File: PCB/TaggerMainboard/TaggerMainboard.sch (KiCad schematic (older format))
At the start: 80 parts

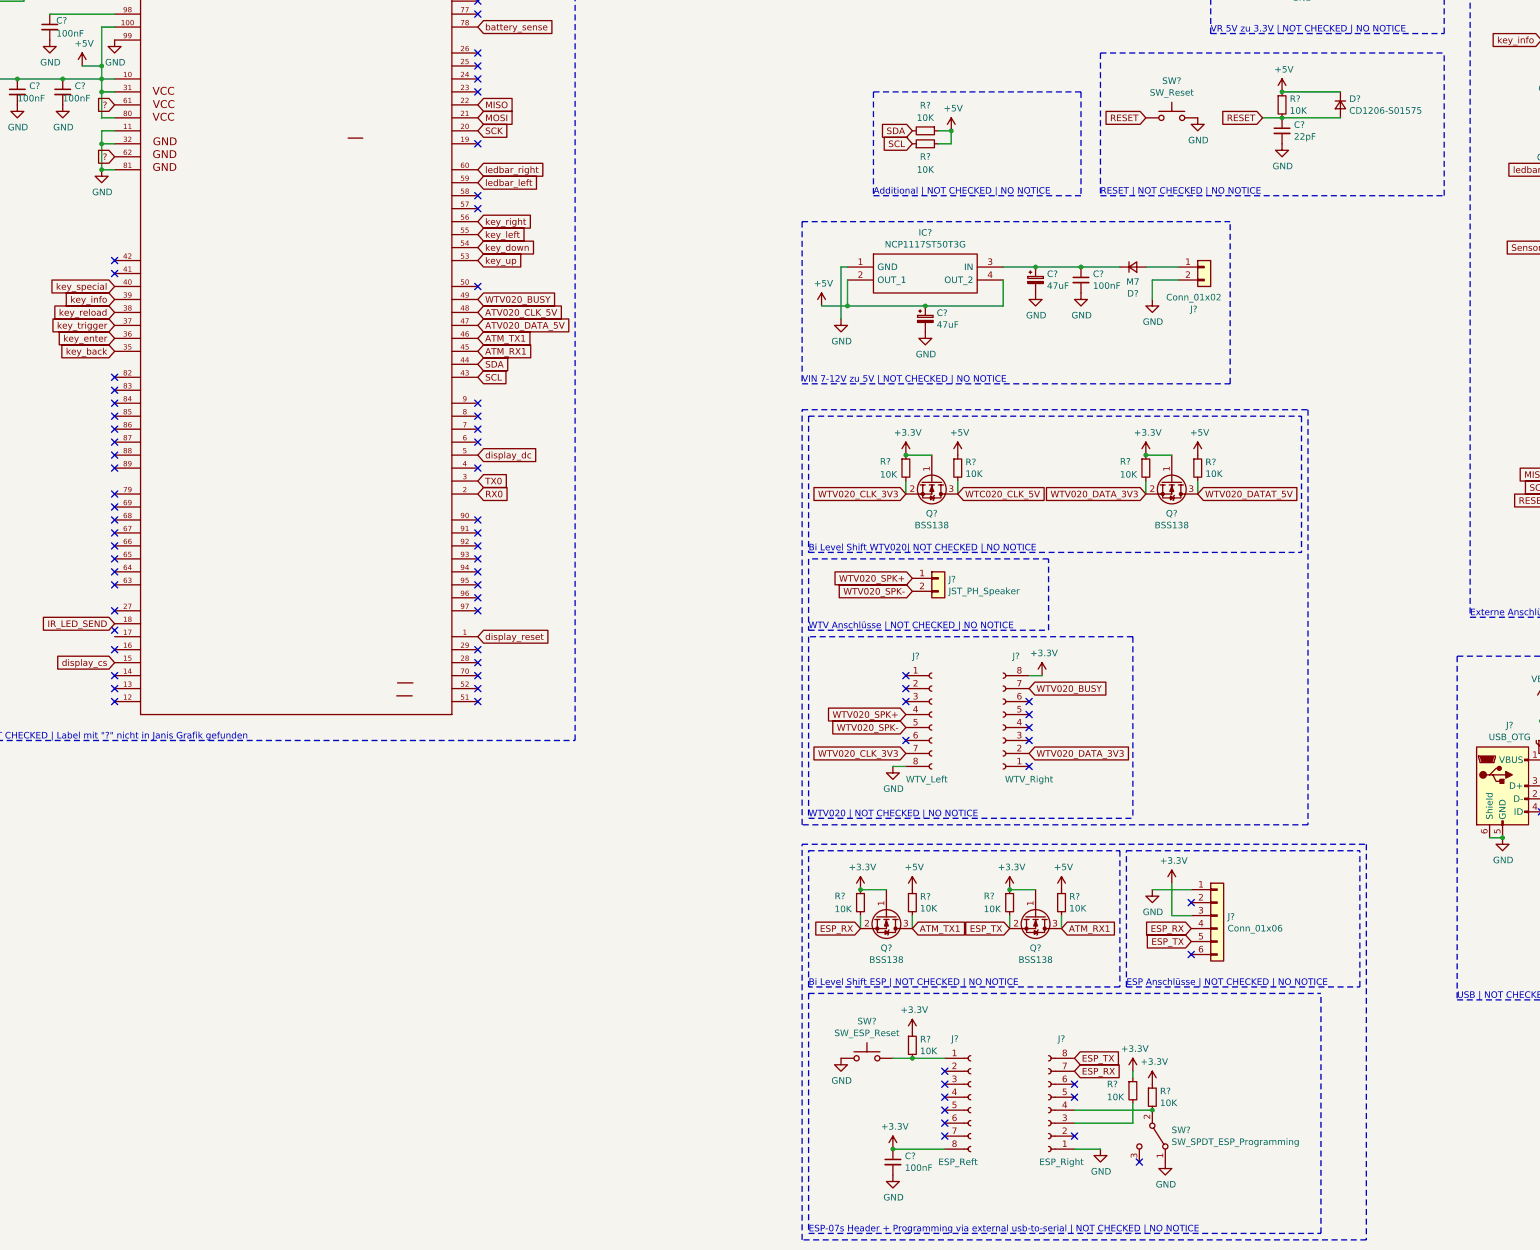
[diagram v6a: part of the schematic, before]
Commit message: VIN ersetzt + WiFi Entfernt + WiFi Header hinzugefügt
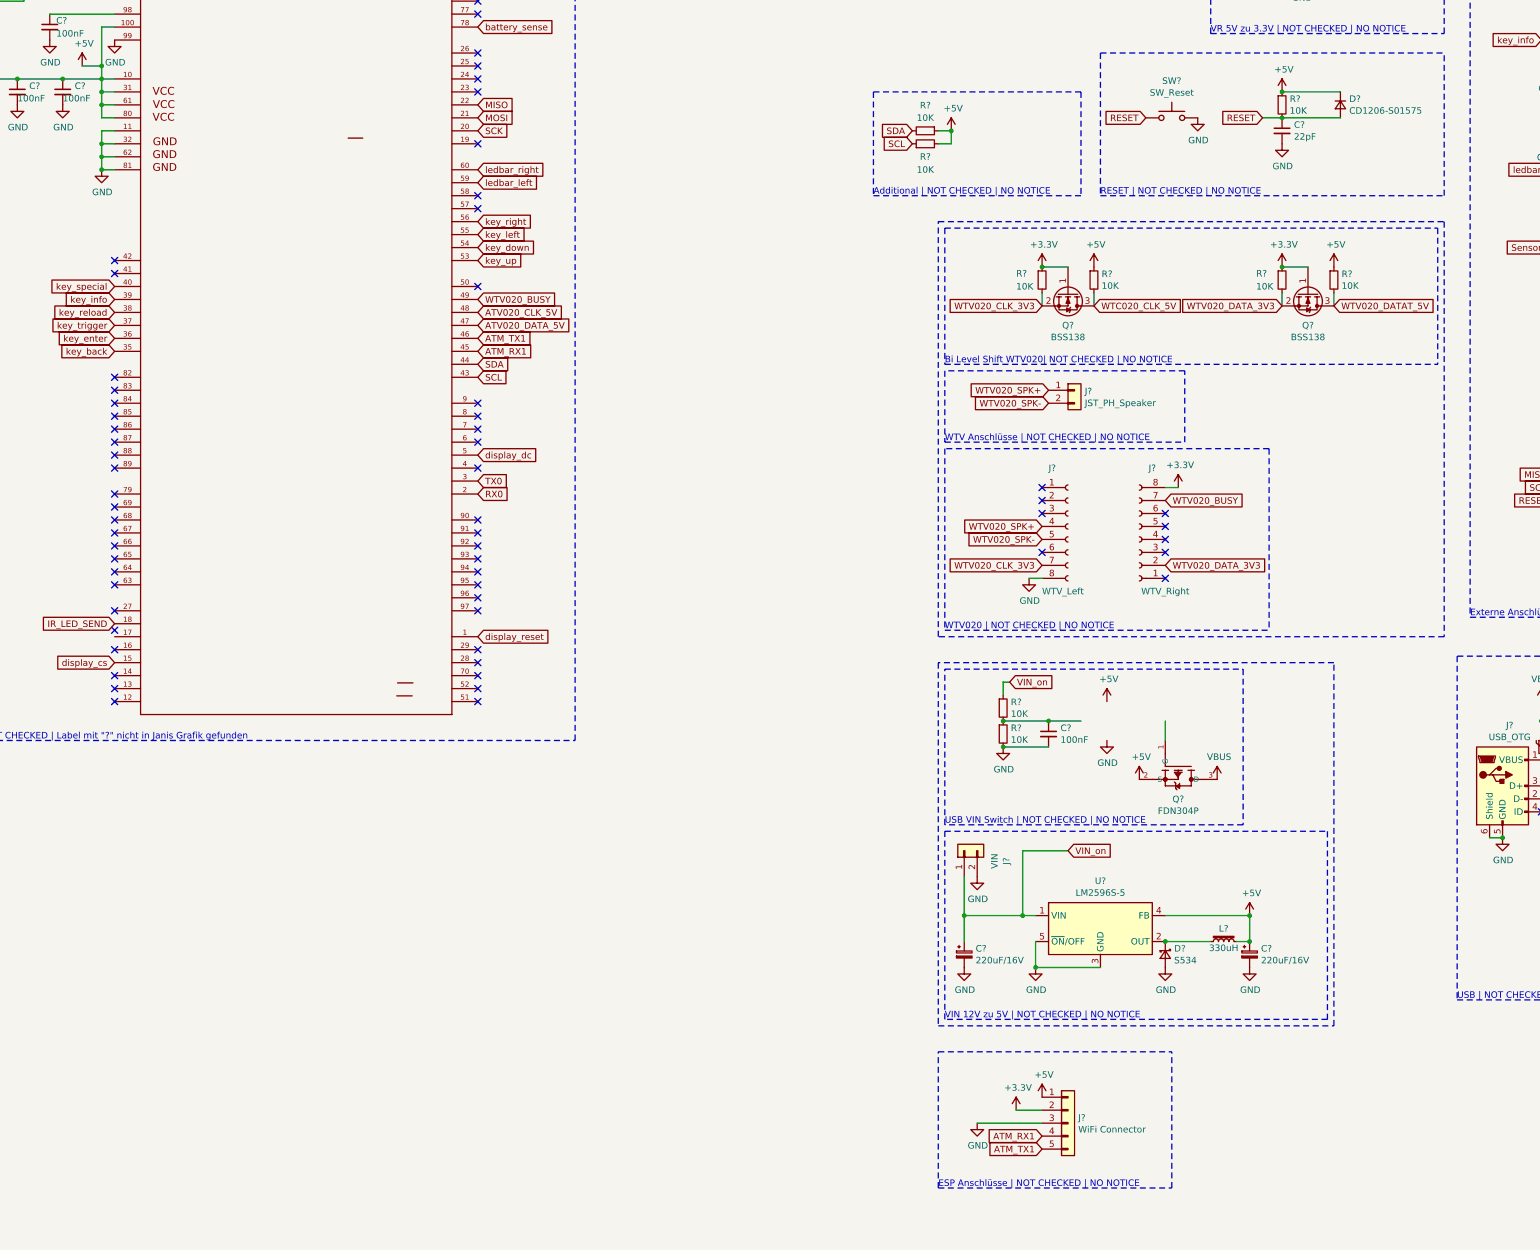
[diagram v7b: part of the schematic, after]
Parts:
- removed C? (x2): 100nF, Capacitor_SMD:C_0805_2012Metric, symbol Device:C_Small
- removed C? (x2): 47uF, Capacitor_SMD:CP_Elec_6.3x5.7, symbol Device:CP_Small
- removed D?: M7, Diode_SMD:D_0805_2012Metric, symbol Device:D_Small
- removed IC?: NCP1117ST50T3G, SOT230P700X180-4N, symbol Infinitag:NCP1117ST50T3G
- removed J?: ESP_Reft, symbol Connector:Conn_01x08_Female
- removed J?: ESP_Right, symbol Connector:Conn_01x08_Female
- removed J?: Conn_01x06, Connector_JST:JST_PH_B6B-PH-K_1x06_P2.00mm_Vertical, symbol Connector_Generic:Conn_01x06
- removed J?: Conn_01x02, Connector_JST:JST_PH_B2B-PH-K_1x02_P2.00mm_Vertical, symbol Connector_Generic:Conn_01x02
- removed Q? (x2): BSS138, Package_TO_SOT_SMD:SOT-23, symbol Transistor_FET:BSS138
- removed R? (x7): 10K, Resistor_SMD:R_0805_2012Metric, symbol Device:R_Small
- removed SW?: SW_ESP_Reset, Button_Switch_SMD:SW_SPST_FSMSM, symbol Switch:SW_Push
- removed SW?: SW_SPDT_ESP_Programming, symbol Switch:SW_SPDT
- added C? (x2): 220uF/16V, symbol Device:CP_Small
- added C?: 100nF, symbol Device:C_Small
- added D?: S534, symbol Device:D_Schottky_Small
- added J?: WiFi Connector, symbol Connector_Generic:Conn_01x05
- added J?: VIN, Connector_JST:JST_PH_B2B-PH-K_1x02_P2.00mm_Vertical, symbol Connector_Generic:Conn_01x02
- added L?: 330uH, symbol Device:L_Core_Iron_Small
- added Q?: FDN304P, SOT95P240X120-3N, symbol FDN340P:FDN340P
- added R? (x2): 10K, symbol Device:R_Small
- added U?: LM2596S-5, Package_TO_SOT_SMD:TO-263-5_TabPin3, symbol Regulator_Switching:LM2596S-5
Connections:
- net labels added: VIN_on
- net labels removed: ?, ESP_RX, ESP_TX
- wire segments 118 -> 112
- no-connect marks 90 -> 78
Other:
- note added: "USB VIN Switch | NOT CHECKED | NO NOTICE"
- note added: "VIN 12V zu 5V | NOT CHECKED | NO NOTICE"
- note removed: "Bi Level Shift ESP | NOT CHECKED | NO NOTICE"
- note removed: "ESP-07s Header + Programming via external usb-to-serial | NOT CHECKED | NO NOTICE"
- note removed: "VIN 7-12V zu 5V | NOT CHECKED | NO NOTICE"
- moved on the sheet: J?, Q?, R?

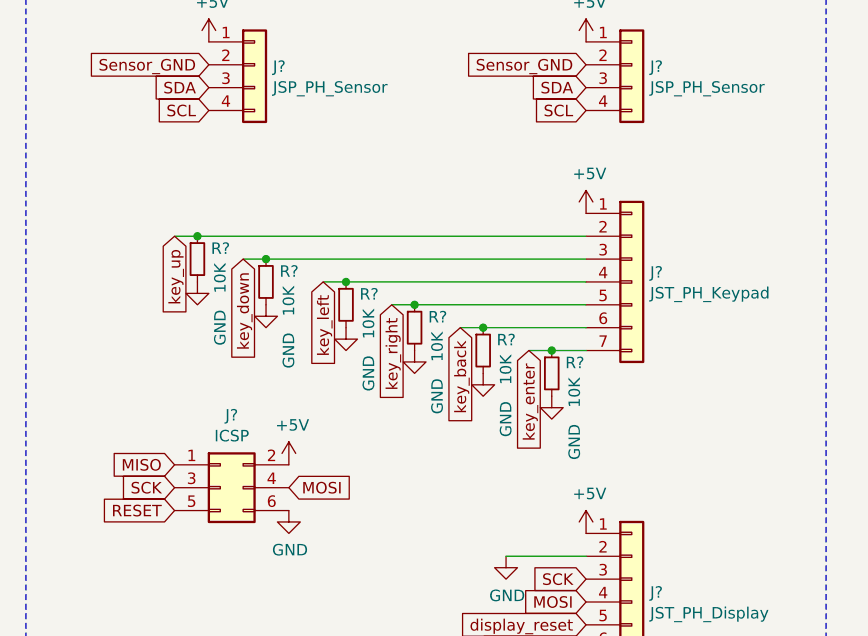
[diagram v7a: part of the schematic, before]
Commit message: Keypad ohne Widerstände auf dem Board
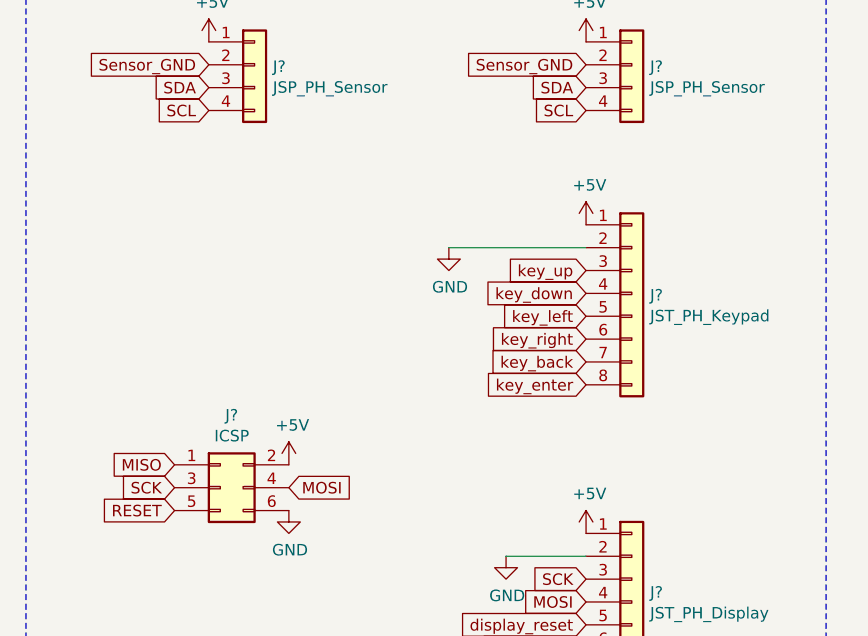
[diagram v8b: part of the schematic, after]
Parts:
- removed J?: JST_PH_Keypad, Connector_JST:JST_PH_B7B-PH-K_1x07_P2.00mm_Vertical, symbol Connector_Generic:Conn_01x07
- removed R? (x6): 10K, Resistor_SMD:R_0805_2012Metric, symbol Device:R_Small
- added J?: JST_PH_Keypad, symbol Connector_Generic:Conn_01x08
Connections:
- wire segments 112 -> 101
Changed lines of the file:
@@
 Text GLabel 13250 3650 0    50   Input ~ 0
 SCL
-$Comp
-L Connector_Generic:Conn_01x07 J?
-U 1 1 5C86ACB0
-P 15100 4400
-F 0 "J?" H 15180 4442 50  0000 L CNN
-F 1 "JST_PH_Keypad" H 15180 4351 50  0000 L CNN
-F 2 "Connector_JST:JST_PH_B7B-PH-K_1x07_P2.00mm_Vertical" H 15100 4400 50  0001 C CNN
-F 3 "~" H 15100 4400 50  0001 C CNN
-	1    15100 4400
-	1    0    0    -1
-$EndComp
-$Comp
-L Device:R_Small R?
-U 1 1 5C86ADDB
-P 14750 4800
-F 0 "R?" H 14809 4846 50  0000 L CNN
-F 1 "10K" V 14850 4650 50  0000 L CNN
-F 2 "Resistor_SMD:R_0805_2012Metric" H 14750 4800 50  0001 C CNN
-F 3 "~" H 14750 4800 50  0001 C CNN
-	1    14750 4800
-	1    0    0    -1
-$EndComp
-$Comp
-L power:GND #PWR?
-U 1 1 5C86AF22
-P 14750 4900
-F 0 "#PWR?" H 14750 4650 50  0001 C CNN
-F 1 "GND" V 14850 4700 50  0000 C CNN
-F 2 "" H 14750 4900 50  0001 C CNN
-F 3 "" H 14750 4900 50  0001 C CNN
-	1    14750 4900
-	1    0    0    -1
-$EndComp
-Text GLabel 14650 4700 3    50   Input ~ 0
+Text GLabel 14900 4850 0    50   Input ~ 0
 key_enter
-Wire Wire Line
-	14900 4700 14750 4700
-Wire Wire Line
-	14650 4700 14750 4700
-Connection ~ 14750 4700
-$Comp
-L Device:R_Small R?
-U 1 1 5C86EFD0
-P 14450 4700
-F 0 "R?" H 14509 4746 50  0000 L CNN
-F 1 "10K" V 14550 4550 50  0000 L CNN
-F 2 "Resistor_SMD:R_0805_2012Metric" H 14450 4700 50  0001 C CNN
-F 3 "~" H 14450 4700 50  0001 C CNN
-	1    14450 4700
-	1    0    0    -1
-$EndComp
-$Comp
-L power:GND #PWR?
-U 1 1 5C86EFD7
-P 14450 4800
-F 0 "#PWR?" H 14450 4550 50  0001 C CNN
-F 1 "GND" V 14550 4600 50  0000 C CNN
-F 2 "" H 14450 4800 50  0001 C CNN
-F 3 "" H 14450 4800 50  0001 C CNN
-	1    14450 4800
-	1    0    0    -1
-$EndComp
-Text GLabel 14350 4600 3    50   Input ~ 0
+Text GLabel 14900 4750 0    50   Input ~ 0
 key_back
-Wire Wire Line
-	14350 4600 14450 4600
-Connection ~ 14450 4600
-$Comp
-L Device:R_Small R?
-U 1 1 5C86F8EF
-P 14150 4600
-F 0 "R?" H 14209 4646 50  0000 L CNN
-F 1 "10K" V 14250 4450 50  0000 L CNN
-F 2 "Resistor_SMD:R_0805_2012Metric" H 14150 4600 50  0001 C CNN
-F 3 "~" H 14150 4600 50  0001 C CNN
-	1    14150 4600
-	1    0    0    -1
-$EndComp
-$Comp
-L power:GND #PWR?
-U 1 1 5C86F8F6
-P 14150 4700
-F 0 "#PWR?" H 14150 4450 50  0001 C CNN
-F 1 "GND" V 14250 4500 50  0000 C CNN
-F 2 "" H 14150 4700 50  0001 C CNN
-F 3 "" H 14150 4700 50  0001 C CNN
-	1    14150 4700
-	1    0    0    -1
-$EndComp
-Text GLabel 14050 4500 3    50   Input ~ 0
+Text GLabel 14900 4650 0    50   Input ~ 0
 key_right
-Wire Wire Line
-	14050 4500 14150 4500
-Connection ~ 14150 4500
-$Comp
-L Device:R_Small R?
-U 1 1 5C87034B
-P 13850 4500
-F 0 "R?" H 13909 4546 50  0000 L CNN
-F 1 "10K" V 13950 4350 50  0000 L CNN
-F 2 "Resistor_SMD:R_0805_2012Metric" H 13850 4500 50  0001 C CNN
-F 3 "~" H 13850 4500 50  0001 C CNN
-	1    13850 4500
-	1    0    0    -1
-$EndComp
-$Comp
-L power:GND #PWR?
-U 1 1 5C870352
-P 13850 4600
-F 0 "#PWR?" H 13850 4350 50  0001 C CNN
-F 1 "GND" V 13950 4400 50  0000 C CNN
-F 2 "" H 13850 4600 50  0001 C CNN
-F 3 "" H 13850 4600 50  0001 C CNN
-	1    13850 4600
-	1    0    0    -1
-$EndComp
-Text GLabel 13750 4400 3    50   Input ~ 0
+Text GLabel 14900 4550 0    50   Input ~ 0
 key_left
-Wire Wire Line
-	13750 4400 13850 4400
-Connection ~ 13850 4400
-$Comp
-L Device:R_Small R?
-U 1 1 5C870F04
-P 13500 4400
-F 0 "R?" H 13559 4446 50  0000 L CNN
-F 1 "10K" V 13600 4250 50  0000 L CNN
-F 2 "Resistor_SMD:R_0805_2012Metric" H 13500 4400 50  0001 C CNN
-F 3 "~" H 13500 4400 50  0001 C CNN
-	1    13500 4400
-	1    0    0    -1
-$EndComp
-$Comp
-L power:GND #PWR?
-U 1 1 5C870F0B
-P 13500 4500
-F 0 "#PWR?" H 13500 4250 50  0001 C CNN
-F 1 "GND" V 13600 4300 50  0000 C CNN
-F 2 "" H 13500 4500 50  0001 C CNN
-F 3 "" H 13500 4500 50  0001 C CNN
-	1    13500 4500
-	1    0    0    -1
-$EndComp
-Text GLabel 13400 4300 3    50   Input ~ 0
+Text GLabel 14900 4450 0    50   Input ~ 0
 key_down
-Wire Wire Line
-	13400 4300 13500 4300
-Connection ~ 13500 4300
-$Comp
-L Device:R_Small R?
-U 1 1 5C872016
-P 13200 4300
-F 0 "R?" H 13259 4346 50  0000 L CNN
-F 1 "10K" V 13300 4150 50  0000 L CNN
-F 2 "Resistor_SMD:R_0805_2012Metric" H 13200 4300 50  0001 C CNN
-F 3 "~" H 13200 4300 50  0001 C CNN
-	1    13200 4300
-	1    0    0    -1
-$EndComp
-$Comp
-L power:GND #PWR?
-U 1 1 5C87201D
-P 13200 4400
-F 0 "#PWR?" H 13200 4150 50  0001 C CNN
-F 1 "GND" V 13300 4200 50  0000 C CNN
-F 2 "" H 13200 4400 50  0001 C CNN
-F 3 "" H 13200 4400 50  0001 C CNN
-	1    13200 4400
-	1    0    0    -1
-$EndComp
-Text GLabel 13100 4200 3    50   Input ~ 0
+Text GLabel 14900 4350 0    50   Input ~ 0
 key_up
-Wire Wire Line
-	13100 4200 13200 4200
-Connection ~ 13200 4200
-Wire Wire Line
-	13200 4200 14900 4200
-Wire Wire Line
-	13500 4300 14900 4300
-Wire Wire Line
-	13850 4400 14900 4400
-Wire Wire Line
-	14150 4500 14900 4500
-Wire Wire Line
-	14450 4600 14900 4600
 $Comp
 L power:+5V #PWR?
 U 1 1 5C877906
-P 14900 4100
-F 0 "#PWR?" H 14900 3950 50  0001 C CNN
-F 1 "+5V" H 14915 4273 50  0000 C CNN
-F 2 "" H 14900 4100 50  0001 C CNN
-F 3 "" H 14900 4100 50  0001 C CNN
-	1    14900 4100
+P 14900 4150
+F 0 "#PWR?" H 14900 4000 50  0001 C CNN
+F 1 "+5V" H 14915 4323 50  0000 C CNN
+F 2 "" H 14900 4150 50  0001 C CNN
+F 3 "" H 14900 4150 50  0001 C CNN
+	1    14900 4150
 	1    0    0    -1
 $EndComp
@@
 Wire Notes Line
 	11400 6650 8350 6650
+$Comp
+L Connector_Generic:Conn_01x08 J?
+U 1 1 5C9BDB9F
+P 15100 4450
+F 0 "J?" H 15180 4442 50  0000 L CNN
+F 1 "JST_PH_Keypad" H 15180 4351 50  0000 L CNN
+F 2 "" H 15100 4450 50  0001 C CNN
+F 3 "~" H 15100 4450 50  0001 C CNN
+	1    15100 4450
+	1    0    0    -1
+$EndComp
+$Comp
+L power:GND #PWR?
+U 1 1 5C9CAE21
+P 14300 4250
+F 0 "#PWR?" H 14300 4000 50  0001 C CNN
+F 1 "GND" H 14305 4077 50  0000 C CNN
+F 2 "" H 14300 4250 50  0001 C CNN
+F 3 "" H 14300 4250 50  0001 C CNN
+	1    14300 4250
+	1    0    0    -1
+$EndComp
+Wire Wire Line
+	14300 4250 14900 4250
 $EndSCHEMATC
